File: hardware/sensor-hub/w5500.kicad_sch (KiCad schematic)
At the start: 34 parts, among them J3 RJ45_Wuerth_7499010121A, U2 W5500, Y1 25MHz

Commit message: Add sensors, connectors
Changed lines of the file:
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@@
 		(at 153.67 86.36)
-	)
-	(bus_entry
-		(at 96.52 20.32)
-		(size 2.54 2.54)
-		(stroke
-			(width 0)
-			(type default)
-		)
 	)
 	(wire

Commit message: Change crystal packages, assign footprints
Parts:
- removed Y1: 25MHz, symbol Device:Crystal
- added C36, C37: 18n, Capacitor_SMD:C_0603_1608Metric, symbol Device:C_Small
- added Y1: 25MHz, symbol Device:Crystal_GND24_Small
- C1: value 10nF -> 10n; footprint (none) -> Capacitor_SMD:C_0603_1608Metric
- C15, C17: value 10uF -> 10u; footprint (none) -> Capacitor_SMD:C_0805_2012Metric
- C16, C18, C19, C20, C21, C3, C4, C5, C6: footprint (none) -> Capacitor_SMD:C_0603_1608Metric
- C2: value 4.7uF -> 4.7u; footprint (none) -> Capacitor_SMD:C_0603_1608Metric
- C7: footprint (none) -> Capacitor_SMD:C_1206_3216Metric
- FB1: footprint (none) -> Inductor_SMD:L_0603_1608Metric
- JP1, JP2, JP3: footprint (none) -> Jumper:SolderJumper-3_P1.3mm_Bridged12_RoundedPad1.0x1.5mm
- R1, R10, R11, R2, R3, R31, R32, R4, R5, R6, R7, R8, R9: footprint (none) -> Resistor_SMD:R_0603_1608Metric
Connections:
- net GND: now also C36.2, C37.2, Y1.2, Y1.4
- net at R11.2, U2.30 (XI/CLKIN): now also C37.1, Y1.3
- net at R11.1, U2.31 (XO): now also C36.1, Y1.1
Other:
- moved on the sheet: C17, R11

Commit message: Assign remaining footprints, change HT sensor
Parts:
- Y1: footprint (none) -> Crystal:Crystal_SMD_SeikoEpson_TSX3225-4Pin_3.2x2.5mm
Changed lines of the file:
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@@
 			)
 		)
-		(property "Footprint" ""
+		(property "Footprint" "Crystal:Crystal_SMD_SeikoEpson_TSX3225-4Pin_3.2x2.5mm"
 			(at 100.33 85.09 0)
 			(effects

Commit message: Start layout
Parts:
- added R36, R37: 0R, Resistor_SMD:R_0603_1608Metric, symbol Device:R_Small
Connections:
- net ACT_LED: now also R37.1; no longer J3.9
- net LINK_LED: now also R36.1; no longer J3.11
- net ETH_TXN: now reaches J3.3 (TD-), R3.2, R8.2
- net RXP: now reaches C3.1, R4.2, R7.1
- net ETH_RXP: now reaches C3.2, J3.4 (RD+)
- net ETH_TXP: now reaches J3.1 (TD+), R2.2, R9.2
- net RXN: now reaches C4.1, R5.2, R6.2
- net ETH_RXN: now reaches C4.2, J3.6 (RD-)
- new net: J3.9, R37.2
- new net: J3.11, R36.2

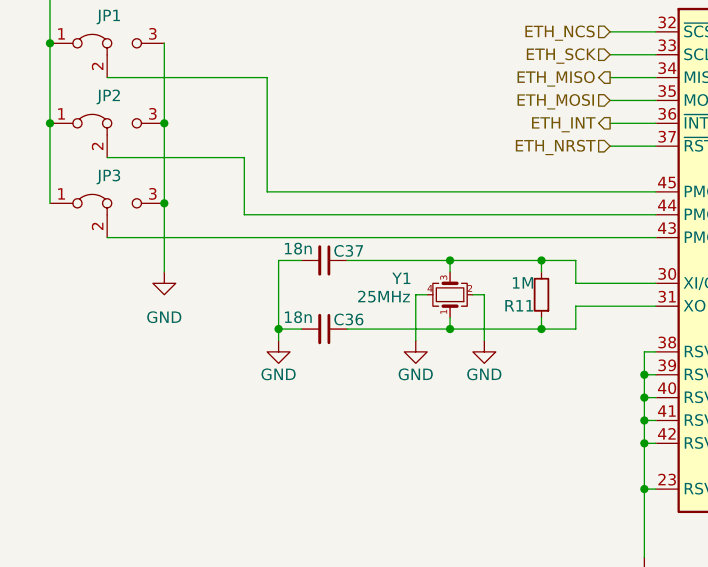
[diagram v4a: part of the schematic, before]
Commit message: V1.0
Fixed value typos, replaced vias with 0.3/0.45, added production files
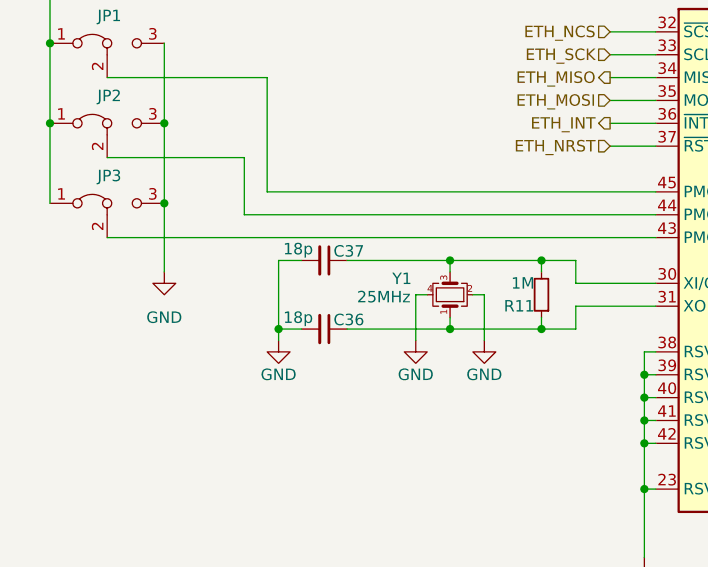
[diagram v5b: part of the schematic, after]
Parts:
- C36, C37: value 18n -> 18p
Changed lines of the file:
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@@
 			)
 		)
-		(property "Value" "18n"
+		(property "Value" "18p"
 			(at 81.788 87.63 90)
 			(effects
@@
 			)
 		)
-		(property "Value" "18n"
+		(property "Value" "18p"
 			(at 81.788 80.01 90)
 			(effects
